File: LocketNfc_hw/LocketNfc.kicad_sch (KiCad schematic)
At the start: 168 parts, among them M1 MOTOR_NO_CONTACTS, Q1 IRLML6401, Q2 IRLML6401, Q3 LED_RGB 5050, Q4 IRLML2030, SW1 SWITCH, SW2 IT1198, SW3 IT1198, SW4 IT1198

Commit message: Placement in progress
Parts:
- removed C123: 3.3pF, Capacitors:CAP_0402, symbol Tittar_kl:C
- removed L123, L124: 12nH, Inductors:IND_0402, symbol Tittar_kl:L
- removed TP2: TESTPOINT, PCB:TESTPOINT_1MM, symbol pcb_details:TESTPOINT
- added C24: *, Capacitors:CAP_0402, symbol Tittar_kl:C
- added C59, C60: 10u, Capacitors:CAP_0603_Silks, symbol Tittar_kl:C
- added R29, R30: 56k, Resistors:RES_0603, symbol Tittar_kl:R
- added R31, R32: 10k, Resistors:RES_0603, symbol Tittar_kl:R
- ANT1: footprint Antennas:Locket5 -> Antennas:LocketNFC_inverted
- C125: value 12pF -> 100pF; footprint Capacitors:CAP_0603 -> Capacitors:CAP_0402; Dielectric X5R or X7R -> NP0
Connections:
- net RF5 is gone; now on net ANT0: C122.2, L132.1
- net +PWR_ESP: now also C59.1, C60.1, R32.2
- net ANT2: now also C24.1
- net AU_BITCK: now also MDL1.11 (IO26/GPIO26/DAC_2/ADC2_CH9/RTC_GPIO7); no longer MDL1.12 (IO27/GPIO27/ADC2_CH7/TOUCH7/RTC_GPIO17)
- net AU_LRCK: now also MDL1.10 (IO25/GPIO25/DAC_1/ADC2_CH8/RTC_GPIO6); no longer MDL1.11 (IO26/GPIO26/DAC_2/ADC2_CH9/RTC_GPIO7)
- net AU_SDA: now also MDL1.12 (IO27/GPIO27/ADC2_CH7/TOUCH7/RTC_GPIO17); no longer MDL1.8 (IO32/GPIO32/XTAL_32K_P/ADC1_CH4/TOUCH9/RTC_GPIO9)
- net BTN1: now also R30.1
- net BTN3: now also R29.1
- net ESP_AUX: now also MDL1.8 (IO32/GPIO32/XTAL_32K_P/ADC1_CH4/TOUCH9/RTC_GPIO9); no longer MDL1.9 (IO33/GPIO33/XTAL_32K_N/ADC1_CH5/TOUCH8/RTC_GPIO8)
- net ESP_GPIO0: now also R32.1
- net GND: now also C24.2, C59.2, C60.2, R29.2, R30.2, R31.1; no longer MDL1.24 (IO2/GPIO2/ADC2_CH2/TOUCH2/RTC_GPIO12/HSPIWP/HS2_DATA0/SD_DATA0)
- removed net AU_MCLK: DD1.1 (PE2/SAI1MCLKA), DD1.67 (OTG_SOF/LPTIM2_OUT/MCO/T1C1/CK1/PA8), MDL1.10 (IO25/GPIO25/DAC_1/ADC2_CH8/RTC_GPIO6)
- new net: MDL1.24 (IO2/GPIO2/ADC2_CH2/TOUCH2/RTC_GPIO12/HSPIWP/HS2_DATA0/SD_DATA0), R31.2
- no-connect marks 65 -> 68
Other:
- note added: "GPIO15 can be used to supress debug messaging through UART0"
- note removed: "GPIO15 can be used to supress debug messaging throug UART0"
- note removed: "MCO"
- note removed: "SAI_MCLK"
- moved on the sheet: ANT1, C125, C50, L6, TP18, TP3, TP4, TP5

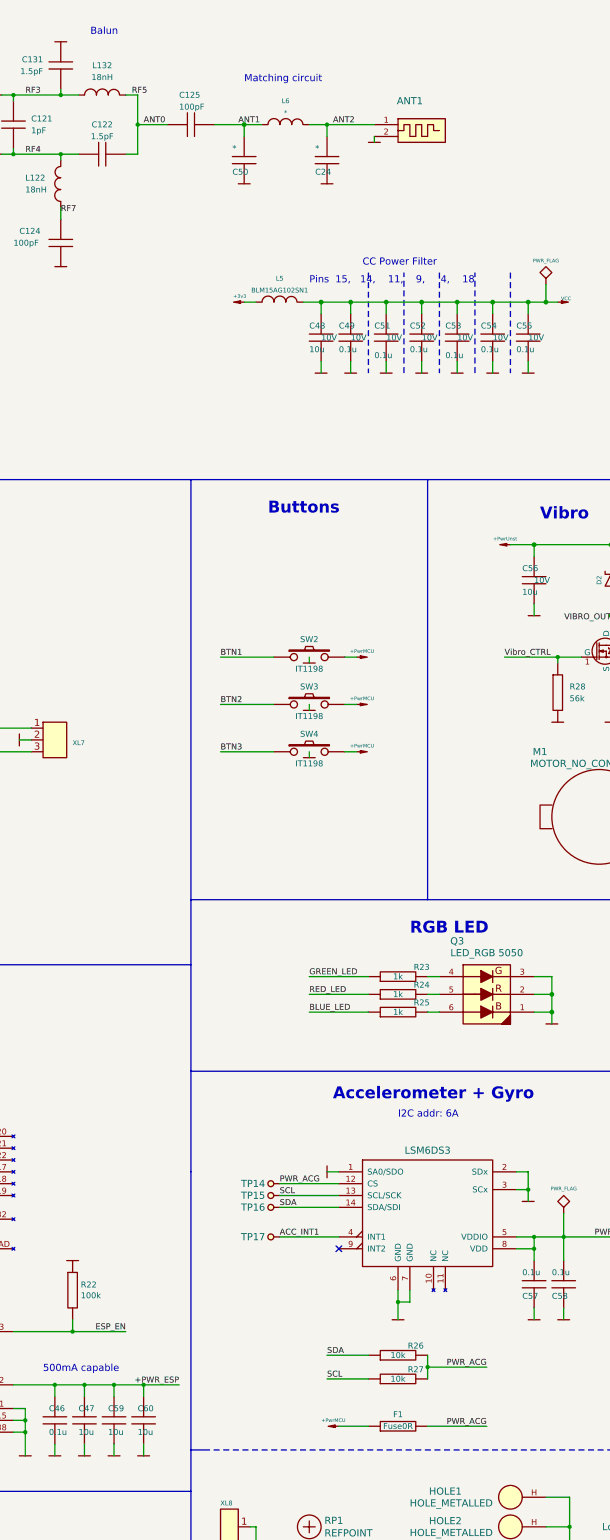
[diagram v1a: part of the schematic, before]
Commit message: Main PCB sent to factory
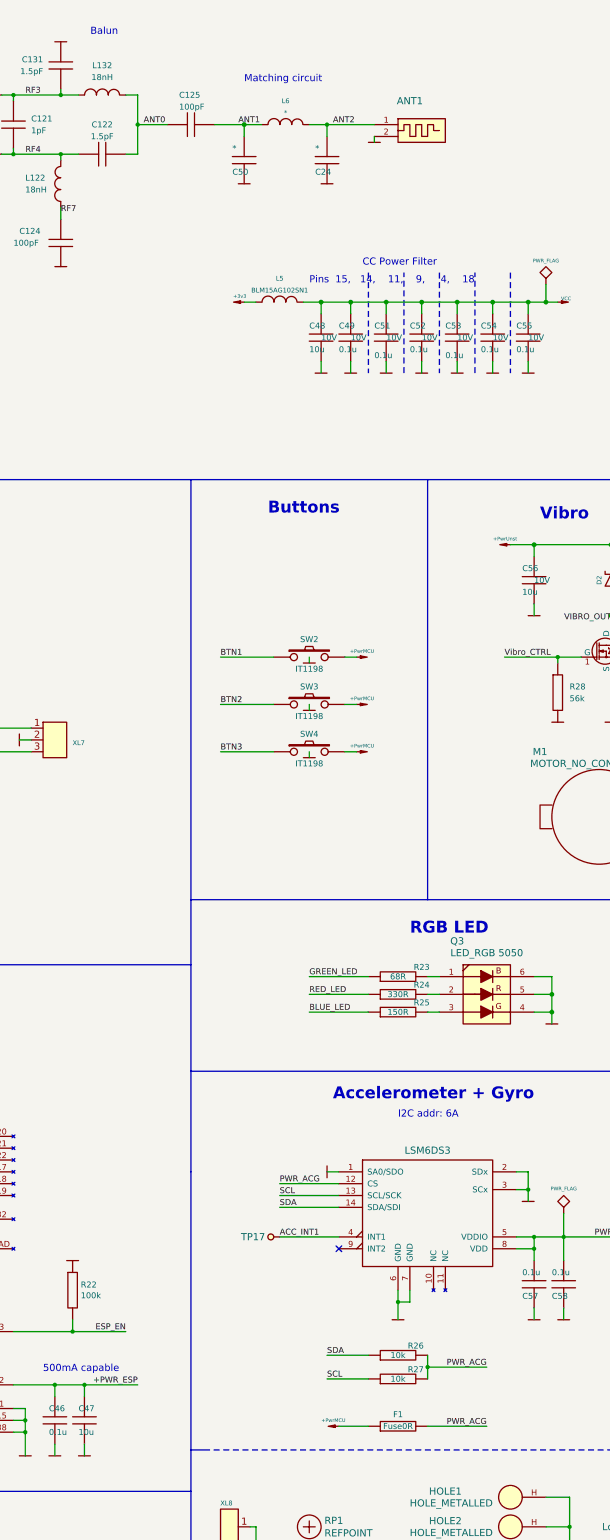
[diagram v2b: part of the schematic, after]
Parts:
- removed C59, C60: 10u, Capacitors:CAP_0603_Silks, symbol Tittar_kl:C
- removed TP14, TP15, TP16: TESTPOINT, PCB:TESTPOINT_1MM, symbol pcb_details:TESTPOINT
- Q3: symbol Tittar_kl:LED_5050_new -> Tittar_kl:LED_5050
- R23: value 1k -> 68R
- R24: value 1k -> 330R
- R25: value 1k -> 150R
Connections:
- net GND: now also Q3.4 (B), Q3.5 (G), Q3.6; no longer Q3.1, Q3.2, Q3.3
- net at R23.2: now also Q3.1; no longer Q3.4 (B)
- net at R25.2: now also Q3.3; no longer Q3.6
- net at R24.2: now also Q3.2; no longer Q3.5 (G)
